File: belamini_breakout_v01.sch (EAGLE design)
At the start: 112 parts, among them IC1 TL074D, IC10 LM4040B10, IC2 LM4041CIDBZ, IC3 TL074D, J1 M10SILK_FEMALE_PTH, SW1 EC12E_SW

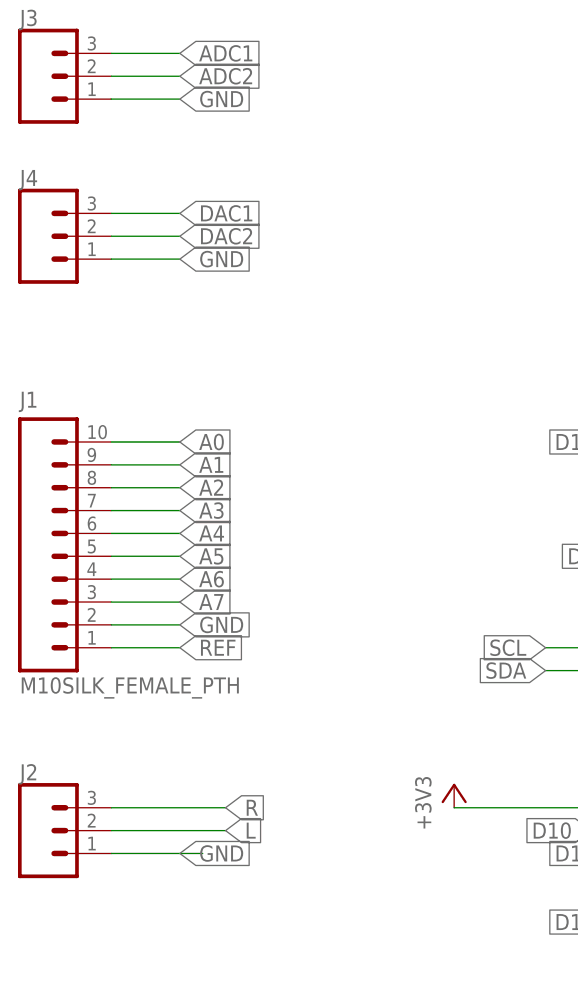
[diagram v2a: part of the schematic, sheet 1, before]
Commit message: Swap output to line out
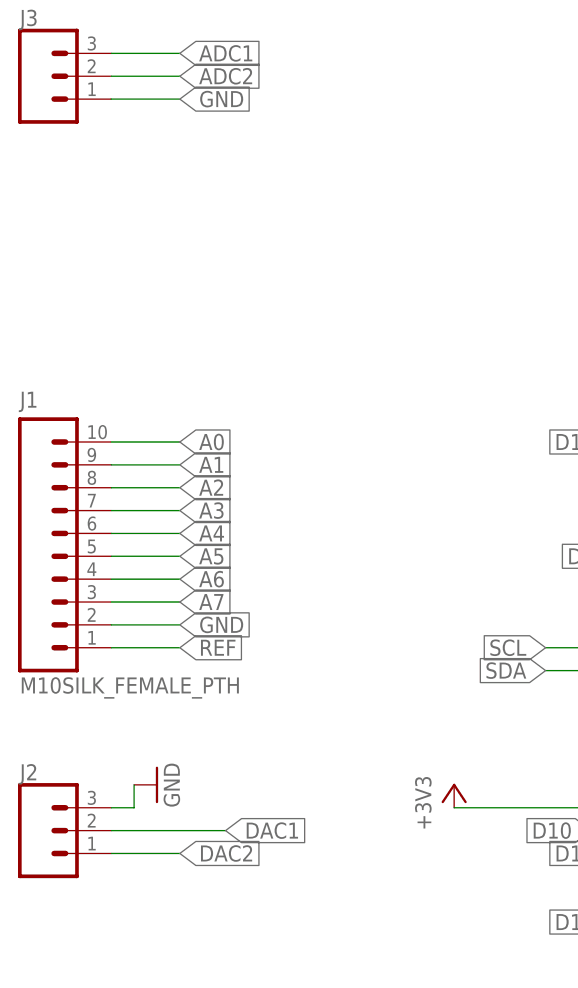
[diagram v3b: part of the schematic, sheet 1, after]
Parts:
- removed J4: (no value), SparkFun-Connectors:CONN_03
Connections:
- removed net L: J2.2
- removed net R: J2.3
- net DAC1: now also J2.2; no longer J4.3
- net DAC2: now also J2.1; no longer J4.2
- net GND: now also J2.3; no longer J2.1, J4.1
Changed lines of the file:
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@@
 <part name="GND22" library="supply1" library_urn="urn:adsk.eagle:library:371" deviceset="GND" device=""/>
 <part name="J3" library="SparkFun-Connectors" library_urn="urn:adsk.eagle:library:513" deviceset="CONN_03" device="" package3d_urn="urn:adsk.eagle:package:38063/1"/>
-<part name="J4" library="SparkFun-Connectors" library_urn="urn:adsk.eagle:library:513" deviceset="CONN_03" device="" package3d_urn="urn:adsk.eagle:package:38063/1"/>
 <part name="SW1" library="switch-alps" library_urn="urn:adsk.eagle:library:373" deviceset="EC12E_SW" device="" package3d_urn="urn:adsk.eagle:package:27083/1"/>
 <part name="GND23" library="supply1" library_urn="urn:adsk.eagle:library:371" deviceset="GND" device=""/>
@@
 <part name="P+19" library="supply1" library_urn="urn:adsk.eagle:library:371" deviceset="+5V" device=""/>
 <part name="P-6" library="supply1" library_urn="urn:adsk.eagle:library:371" deviceset="-12V" device=""/>
+<part name="GND25" library="supply1" library_urn="urn:adsk.eagle:library:371" deviceset="GND" device=""/>
 </parts>
 <sheets>
@@
 <attribute name="NAME" x="63.5" y="99.568" size="1.778" layer="95" font="vector"/>
 </instance>
-<instance part="J4" gate="J$1" x="66.04" y="76.2" smashed="yes">
-<attribute name="VALUE" x="63.5" y="68.834" size="1.778" layer="96" font="vector"/>
-<attribute name="NAME" x="63.5" y="81.788" size="1.778" layer="95" font="vector"/>
-</instance>
 <instance part="+3V10" gate="G$1" x="162.56" y="83.82" smashed="yes">
 <attribute name="VALUE" x="160.02" y="78.74" size="1.778" layer="96" rot="R90"/>
@@
 <instance part="P+19" gate="1" x="160.02" y="68.58" smashed="yes" rot="R270">
 <attribute name="VALUE" x="154.94" y="71.12" size="1.778" layer="96"/>
+</instance>
+<instance part="GND25" gate="1" x="78.74" y="15.24" smashed="yes" rot="R90">
+<attribute name="VALUE" x="81.28" y="12.7" size="1.778" layer="96" rot="R90"/>
 </instance>
 </instances>
@@
 </segment>
 <segment>
-<pinref part="J2" gate="J$1" pin="1"/>
-<wire x1="73.66" y1="7.62" x2="83.82" y2="7.62" width="0.1524" layer="91"/>
-<label x="81.28" y="7.62" size="1.778" layer="95" xref="yes"/>
-</segment>
-<segment>
 <pinref part="J3" gate="J$1" pin="1"/>
 <wire x1="73.66" y1="91.44" x2="81.28" y2="91.44" width="0.1524" layer="91"/>
 <label x="81.28" y="91.44" size="1.778" layer="95" xref="yes"/>
-</segment>
-<segment>
-<pinref part="J4" gate="J$1" pin="1"/>
-<wire x1="73.66" y1="73.66" x2="81.28" y2="73.66" width="0.1524" layer="91"/>
-<label x="81.28" y="73.66" size="1.778" layer="95" xref="yes"/>
 </segment>
 <segment>
@@
 <wire x1="149.86" y1="71.12" x2="187.96" y2="71.12" width="0.1524" layer="91"/>
 </segment>
+<segment>
+<pinref part="J2" gate="J$1" pin="3"/>
+<pinref part="GND25" gate="1" pin="GND"/>
+<wire x1="73.66" y1="12.7" x2="76.2" y2="12.7" width="0.1524" layer="91"/>
+<wire x1="76.2" y1="12.7" x2="76.2" y2="15.24" width="0.1524" layer="91"/>
+</segment>
 </net>
 <net name="REF" class="0">
@@
 </segment>
 </net>
-<net name="R" class="0">
-<segment>
-<pinref part="J2" gate="J$1" pin="3"/>
-<wire x1="73.66" y1="12.7" x2="86.36" y2="12.7" width="0.1524" layer="91"/>
-<label x="86.36" y="12.7" size="1.778" layer="95" xref="yes"/>
-</segment>
-</net>
-<net name="L" class="0">
+<net name="DAC1" class="0">
 <segment>
 <pinref part="J2" gate="J$1" pin="2"/>
@@
 </segment>
 </net>
-<net name="DAC1" class="0">
-<segment>
-<pinref part="J4" gate="J$1" pin="3"/>
-<wire x1="73.66" y1="78.74" x2="81.28" y2="78.74" width="0.1524" layer="91"/>
-<label x="81.28" y="78.74" size="1.778" layer="95" xref="yes"/>
-</segment>
-</net>
-<net name="DAC2" class="0">
-<segment>
-<pinref part="J4" gate="J$1" pin="2"/>
-<wire x1="73.66" y1="76.2" x2="81.28" y2="76.2" width="0.1524" layer="91"/>
-<label x="81.28" y="76.2" size="1.778" layer="95" xref="yes"/>
-</segment>
-</net>
 <net name="SCL" class="0">
 <segment>
@@
 </segment>
 </net>
+<net name="DAC2" class="0">
+<segment>
+<pinref part="J2" gate="J$1" pin="1"/>
+<wire x1="73.66" y1="7.62" x2="81.28" y2="7.62" width="0.1524" layer="91"/>
+<label x="81.28" y="7.62" size="1.778" layer="95" xref="yes"/>
+</segment>
+</net>
